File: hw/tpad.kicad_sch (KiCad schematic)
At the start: 7 parts, among them Q701 2N7002K

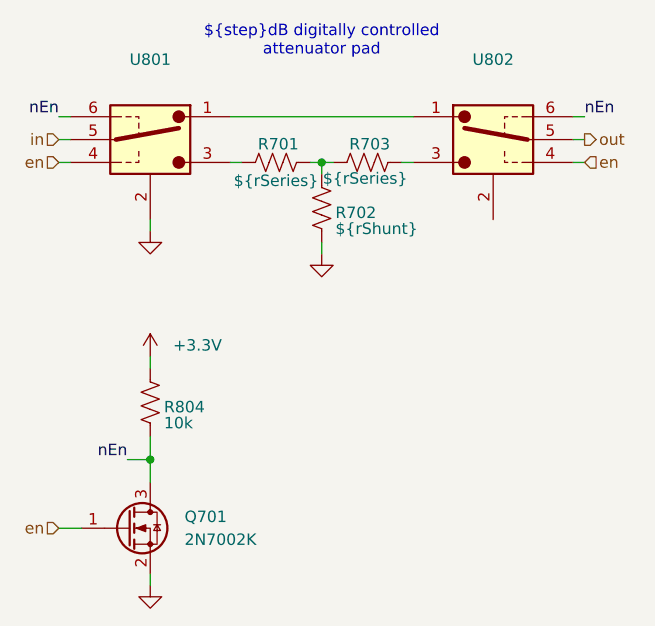
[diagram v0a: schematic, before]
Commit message: "Final" rx preselector design for good digital tuning in 800 ohm domain and general 1MHz..30MHz coverage
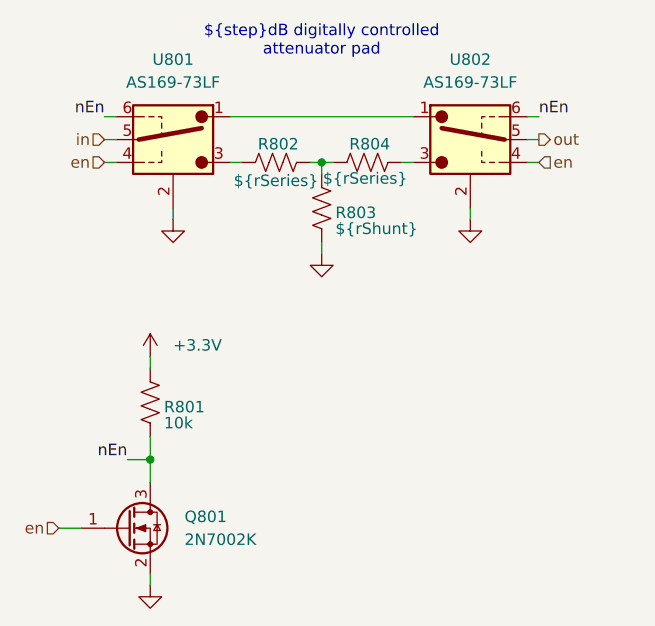
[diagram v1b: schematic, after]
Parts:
- U801, U802: value ~ -> AS169-73LF
- renumbered Q701 to Q801, R804 to R801, R701 to R802, R702 to R803, R703 to R804
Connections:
- net GND: now also U802.2 (GND)
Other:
- moved on the sheet: U801, U802

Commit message: Ready for first schematic review with Claude.ai
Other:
- company: (none) -> WB7NAB
- title: (none) -> Attenuator Tpad
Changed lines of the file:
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@@
 	(generator "eeschema")
 	(generator_version "9.0")
-	(paper "A4")
+	(paper "USLetter")
+	(title_block
+		(title "Attenuator Tpad")
+		(company "WB7NAB")
+		(comment 1 "Alan Mimms")
+	)
 	(text "${step}dB digitally controlled\nattenuator pad"
 		(exclude_from_sim no)

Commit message: After Claude schematic review all issues resolved.
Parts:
- U801, U802: value AS169-73LF -> AS183-92LF
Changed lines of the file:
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@@
 			)
 		)
-		(property "Value" "AS169-73LF"
+		(property "Value" "AS183-92LF"
 			(at 81.28 81.28 0)
 			(effects
@@
 			)
 		)
-		(property "Value" "AS169-73LF"
+		(property "Value" "AS183-92LF"
 			(at 114.3 81.28 0)
 			(effects

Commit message: Starting to assign footprints for remaining components. Adding L1+L2 and L1||L2 relay stuff
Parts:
- U801, U802: footprint (none) -> Library:SOT65P220X110-6N
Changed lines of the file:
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@@
 			)
 		)
-		(property "Footprint" ""
+		(property "Footprint" "Library:SOT65P220X110-6N"
 			(at 81.28 87.63 0)
 			(effects
@@
 			)
 		)
-		(property "Footprint" ""
+		(property "Footprint" "Library:SOT65P220X110-6N"
 			(at 114.3 87.63 0)
 			(effects

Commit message: Thinking and documenting DPD. Working on footprints.
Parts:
- R802, R804: value ${rSeries} -> 34
- R803: value ${rShunt} -> 562

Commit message: All footprints assigned at least on trial basis.
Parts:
- R801: footprint (none) -> Resistor_SMD:R_0603_1608Metric
- R802, R803, R804: footprint (none) -> Resistor_SMD:R_1206_3216Metric
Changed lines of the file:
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@@
 			)
 		)
-		(property "Footprint" ""
+		(property "Footprint" "Resistor_SMD:R_0603_1608Metric"
 			(at 79.756 117.094 90)
 			(effects
@@
 			)
 		)
-		(property "Footprint" ""
+		(property "Footprint" "Resistor_SMD:R_1206_3216Metric"
 			(at 98.806 95.504 90)
 			(effects
@@
 			)
 		)
-		(property "Footprint" ""
+		(property "Footprint" "Resistor_SMD:R_1206_3216Metric"
 			(at 103.124 89.154 90)
 			(effects
@@
 			)
 		)
-		(property "Footprint" ""
+		(property "Footprint" "Resistor_SMD:R_1206_3216Metric"
 			(at 92.456 91.186 90)
 			(effects

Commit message: Switched to LTC3779 for Veer buck/boost to enable 80V Veer for possible 100W support someday.
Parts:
- U801, U802: footprint Library:SOT65P220X110-6N -> SOT65P220X110-6N; Height (none) -> 1.1; Manufacturer_Name (none) -> Skyworks; Manufacturer_Part_Number (none) -> AS183-92LF; Mouser Part Number (none) -> 873-AS183-92LF; Mouser Price/Stock (none) -> https://www.mouser.co.uk/ProductDetail/Skyworks-Solutions-I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
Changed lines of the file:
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@@
 			)
 		)
-		(property "Footprint" "Library:SOT65P220X110-6N"
-			(at 81.28 87.63 0)
-			(effects
-				(font
-					(size 1.27 1.27)
-				)
-				(hide yes)
-			)
-		)
-		(property "Datasheet" ""
-			(at 81.28 87.63 0)
-			(effects
-				(font
-					(size 1.27 1.27)
-				)
-				(hide yes)
-			)
-		)
-		(property "Description" ""
+		(property "Footprint" "SOT65P220X110-6N"
+			(at 59.69 182.55 0)
+			(effects
+				(font
+					(size 1.27 1.27)
+				)
+				(justify left top)
+				(hide yes)
+			)
+		)
+		(property "Datasheet" "https://www.skyworksinc.com/-/media/SkyWorks/Documents/Products/1-100/200177D.pdf"
+			(at 59.69 282.55 0)
+			(effects
+				(font
+					(size 1.27 1.27)
+				)
+				(justify left top)
+				(hide yes)
+			)
+		)
+		(property "Description" "RF Switch ICs .3-2500MHz IL .3dB IP3 +43dBm"
 			(at 81.28 87.63 0)
 			(effects
@@
 					(size 1.27 1.27)
 				)
+				(hide yes)
+			)
+		)
+		(property "Height" "1.1"
+			(at 59.69 482.55 0)
+			(effects
+				(font
+					(size 1.27 1.27)
+				)
+				(justify left top)
+				(hide yes)
+			)
+		)
+		(property "Mouser Part Number" "873-AS183-92LF"
+			(at 59.69 582.55 0)
+			(effects
+				(font
+					(size 1.27 1.27)
+				)
+				(justify left top)
+				(hide yes)
+			)
+		)
+		(property "Mouser Price/Stock" "https://www.mouser.co.uk/ProductDetail/Skyworks-Solutions-Inc/AS183-92LF?qs=WMHGlxXAKT9uKJ5iI33IgQ%3D%3D"
+			(at 59.69 682.55 0)
+			(effects
+				(font
+					(size 1.27 1.27)
+				)
+				(justify left top)
+				(hide yes)
+			)
+		)
+		(property "Manufacturer_Name" "Skyworks"
+			(at 59.69 782.55 0)
+			(effects
+				(font
+					(size 1.27 1.27)
+				)
+				(justify left top)
+				(hide yes)
+			)
+		)
+		(property "Manufacturer_Part_Number" "AS183-92LF"
+			(at 59.69 882.55 0)
+			(effects
+				(font
+					(size 1.27 1.27)
+				)
+				(justify left top)
 				(hide yes)
 			)
@@
 			)
 		)
-		(property "Footprint" "Library:SOT65P220X110-6N"
-			(at 114.3 87.63 0)
-			(effects
-				(font
-					(size 1.27 1.27)
-				)
-				(hide yes)
-			)
-		)
-		(property "Datasheet" ""
-			(at 114.3 87.63 0)
-			(effects
-				(font
-					(size 1.27 1.27)
-				)
-				(hide yes)
-			)
-		)
-		(property "Description" ""
+		(property "Footprint" "SOT65P220X110-6N"
+			(at 135.89 182.55 0)
+			(effects
+				(font
+					(size 1.27 1.27)
+				)
+				(justify left top)
+				(hide yes)
+			)
+		)
+		(property "Datasheet" "https://www.skyworksinc.com/-/media/SkyWorks/Documents/Products/1-100/200177D.pdf"
+			(at 135.89 282.55 0)
+			(effects
+				(font
+					(size 1.27 1.27)
+				)
+				(justify left top)
+				(hide yes)
+			)
+		)
+		(property "Description" "RF Switch ICs .3-2500MHz IL .3dB IP3 +43dBm"
 			(at 114.3 87.63 0)
 			(effects
@@
 				(hide yes)
 			)
+		)
+		(property "Height" "1.1"
+			(at 135.89 482.55 0)
+			(effects
+				(font
+					(size 1.27 1.27)
+				)
+				(justify left top)
+				(hide yes)
+			)
+		)
+		(property "Mouser Part Number" "873-AS183-92LF"
+			(at 135.89 582.55 0)
+			(effects
+				(font
+					(size 1.27 1.27)
+				)
+				(justify left top)
+				(hide yes)
+			)
+		)
+		(property "Mouser Price/Stock" "https://www.mouser.co.uk/ProductDetail/Skyworks-Solutions-Inc/AS183-92LF?qs=WMHGlxXAKT9uKJ5iI33IgQ%3D%3D"
+			(at 135.89 682.55 0)
+			(effects
+				(font
+					(size 1.27 1.27)
+				)
+				(justify left top)
+				(hide yes)
+			)
+		)
+		(property "Manufacturer_Name" "Skyworks"
+			(at 135.89 782.55 0)
+			(effects
+				(font
+					(size 1.27 1.27)
+				)
+				(justify left top)
+				(hide yes)
+			)
+		)
+		(property "Manufacturer_Part_Number" "AS183-92LF"
+			(at 135.89 882.55 0)
+			(effects
+				(font
+					(size 1.27 1.27)
+				)
+				(justify left top)
+				(hide yes)
+			)
